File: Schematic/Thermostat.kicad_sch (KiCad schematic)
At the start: 36 parts, among them J1 Relay conn., J2 Thermocouple, J4 USB_B_Micro, J5 Firmware, K1 SONGLE_SRD_05VDC_SL_C, Q1 BSS138, SW1 Reset, SW2 Temp+, SW3 Preset1, SW4 Temp-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

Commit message: Added status LEDs, changed button functions
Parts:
- added D2: Green, LED_SMD:LED_0603_1608Metric_Pad1.05x0.95mm_HandSolder, symbol Device:LED_Small
- added D3: Red, LED_SMD:LED_0603_1608Metric_Pad1.05x0.95mm_HandSolder, symbol Device:LED_Small
- added H1, H2: MountingHole, MountingHole:MountingHole_3.2mm_M3, symbol Mechanical:MountingHole
- added R23 (x2): 1kΩ, Resistor_SMD:R_0603_1608Metric_Pad0.98x0.95mm_HandSolder, symbol Device:R_Small
- D4: renamed from D3; value "+5V" -> Green
- J5: footprint myDevices:PinHeader_1x06_P2.54mm_Vertical_Minus2 -> Retronics_Connectors:PinHeader_1x06_P2.54mm_Vertical_Minus2
- SW6: value Function -> Enter
- SW7: value Hysteresis -> Setup
- renumbered SW4 to SW3, SW3 to SW4
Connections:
- net GND: now also D2.1 (K), D3.1 (K)
- net LED_TEMP: now reaches U2.25 (A2)
- net LED_TEMP: now also R23.1
- net LED_STATUS: now reaches U2.26 (A3)
- net LED_STATUS: now also R23.1
- net SW_Function renamed SW_Enter
- net SW_Hysteresis renamed SW_Setup
- new net: D3.2 (A), R23.2
- new net: D2.2 (A), R23.2
- no-connect marks 13 -> 11

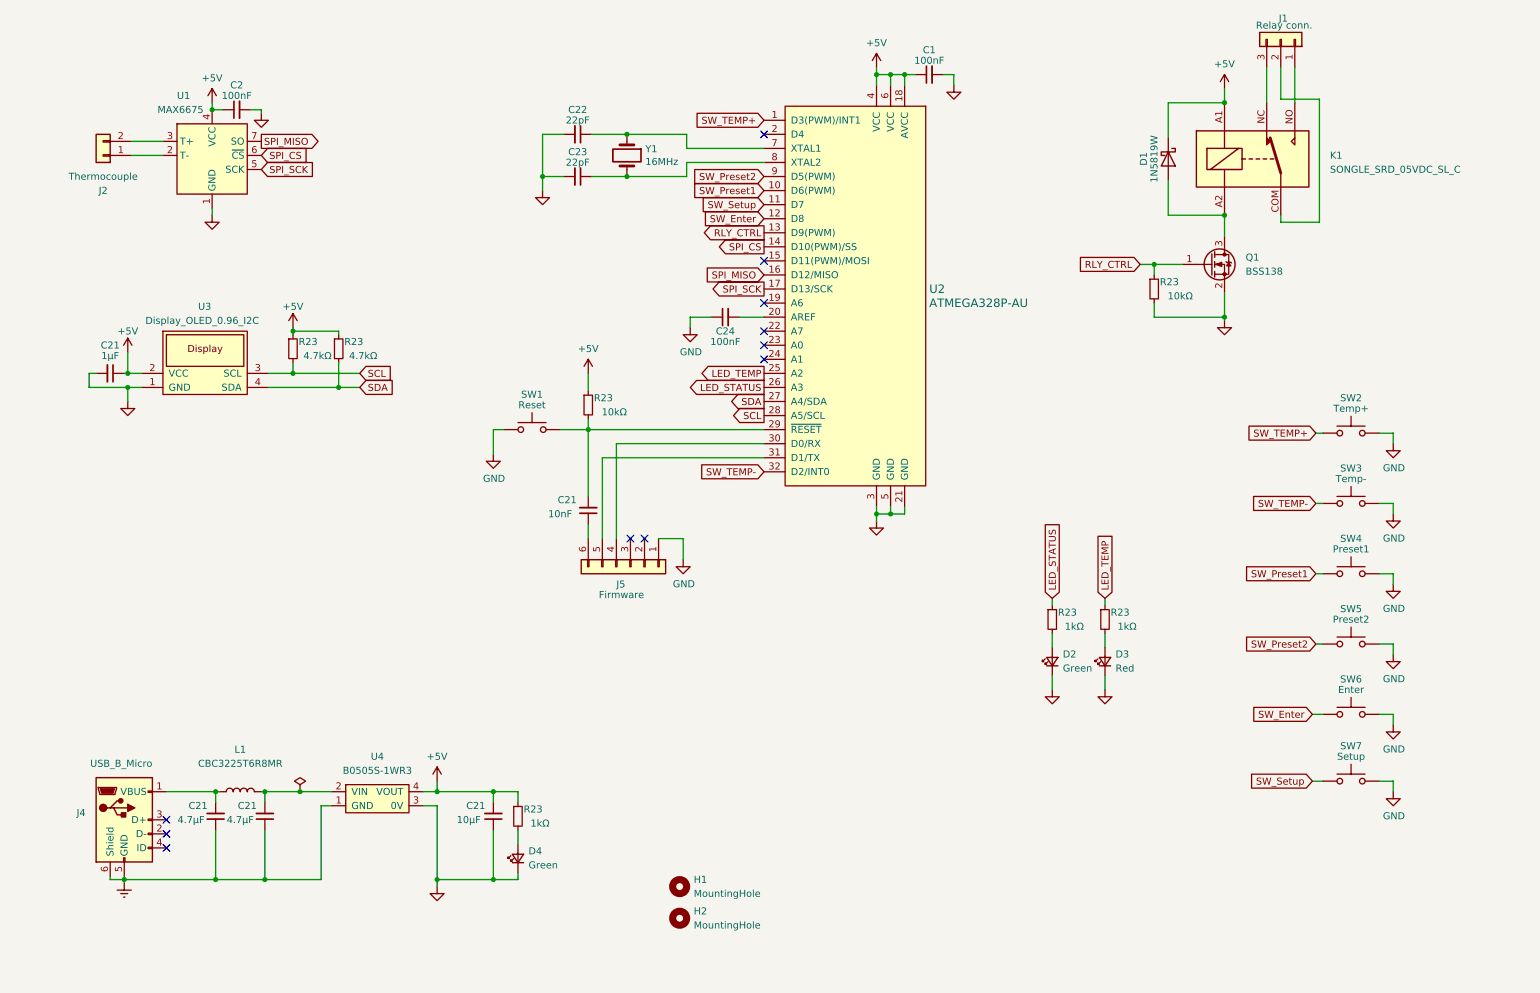
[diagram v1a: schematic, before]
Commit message: Added pull-up/pull-down resistors for sensor, removed redundant LEDs
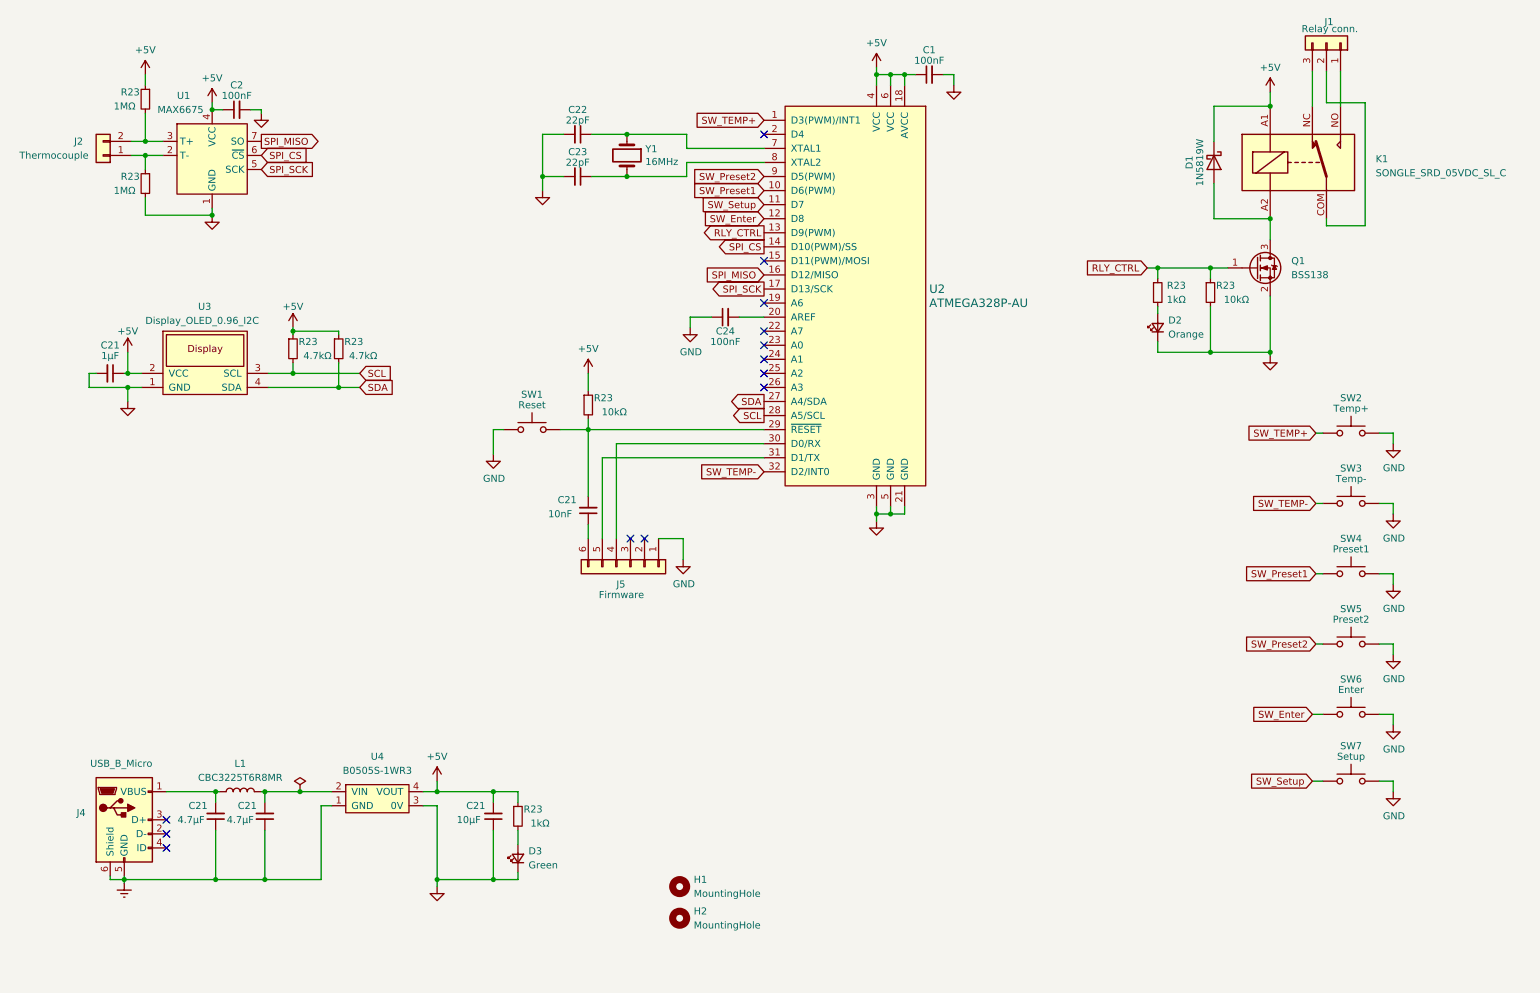
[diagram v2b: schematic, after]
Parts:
- removed D3: Red, LED_SMD:LED_0603_1608Metric_Pad1.05x0.95mm_HandSolder, symbol Device:LED_Small
- removed R23 (x2): 1kΩ, Resistor_SMD:R_0603_1608Metric_Pad0.98x0.95mm_HandSolder, symbol Device:R_Small
- added R23: 1kΩ, Resistor_SMD:R_0603_1608Metric_Pad0.98x0.95mm_HandSolder, symbol Device:R_Small
- added R23 (x2): 1MΩ, Resistor_SMD:R_0603_1608Metric_Pad0.98x0.95mm_HandSolder, symbol Device:R_Small
- D2: value Green -> Orange
- renumbered D4 to D3
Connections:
- net +5V: now also R23.1
- net GND: now also R23.2
- net RLY_CTRL: now also R23.1
- net at D2.2 (A): now also R23.2
- net at J2.1 (Pin_1), U1.2 (T-): now also R23.1
- net at J2.2 (Pin_2), U1.3 (T+): now also R23.2
- net LED_STATUS: no longer names the net of U2.26 (A3)
- net LED_TEMP: no longer names the net of U2.25 (A2)
- no-connect marks 11 -> 13
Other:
- moved on the sheet: D1, J1, K1, Q1, R23

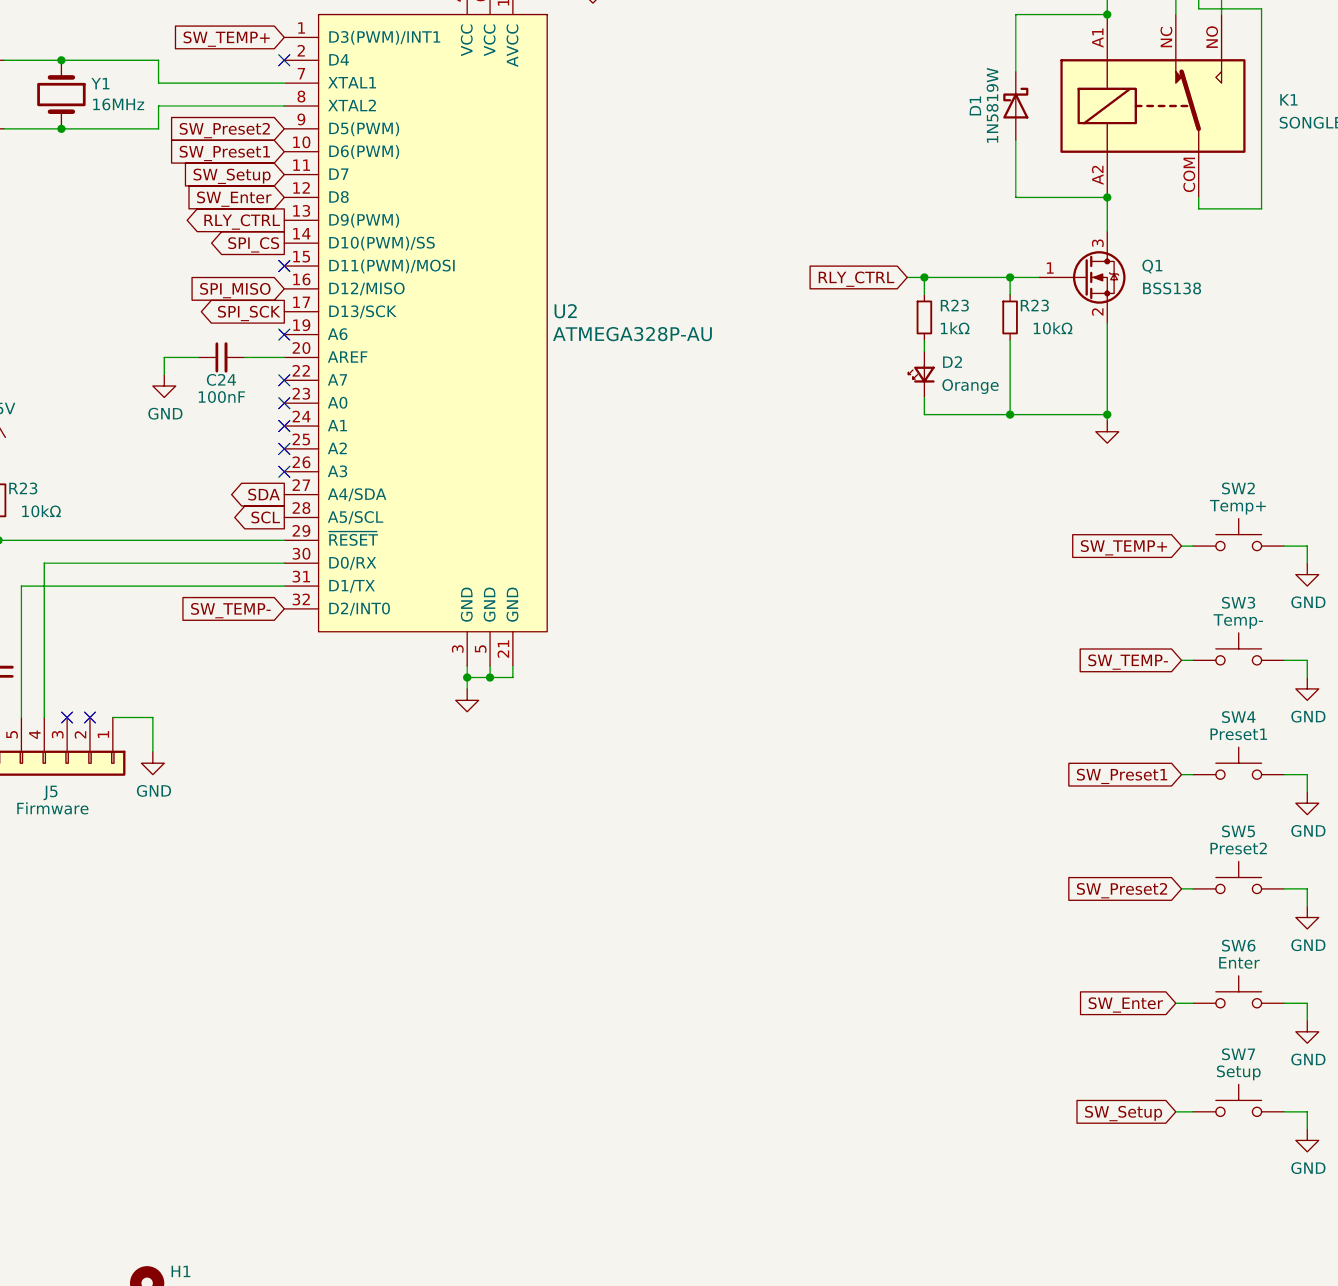
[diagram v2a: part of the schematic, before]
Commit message: Altered button configuration
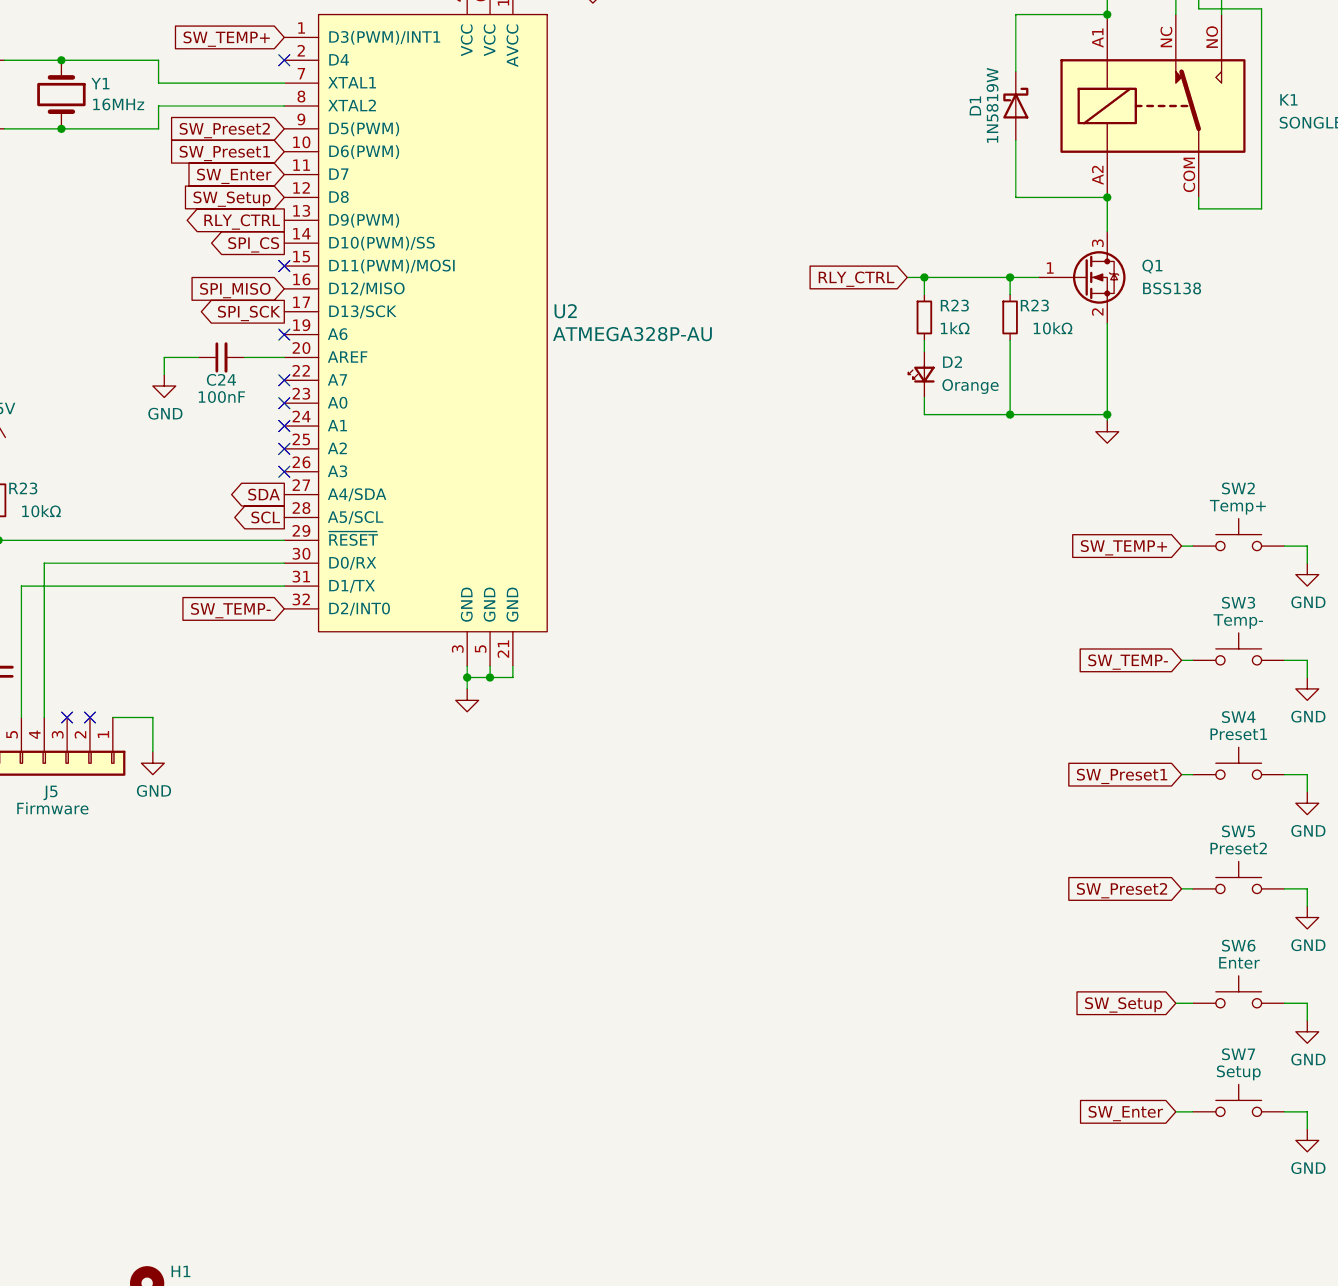
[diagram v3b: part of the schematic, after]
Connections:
- net SW_Enter: now also SW7.1, U2.11 (D7); no longer SW6.1, U2.12 (D8)
- net SW_Setup: now also SW6.1, U2.12 (D8); no longer SW7.1, U2.11 (D7)
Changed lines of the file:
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@@
     )
   )
-  (global_label "SW_Enter" (shape input) (at 149.86 52.07 180) (fields_autoplaced)
+  (global_label "SW_Enter" (shape input) (at 149.86 49.53 180) (fields_autoplaced)
     (effects (font (size 1.27 1.27)) (justify right))
-    (property "Intersheetrefs" "${INTERSHEET_REFS}" (at 138.3478 52.07 0)
+    (property "Intersheetrefs" "${INTERSHEET_REFS}" (at 138.3478 49.53 0)
       (effects (font (size 1.27 1.27)) (justify right) hide)
     )
@@
     )
   )
-  (global_label "SW_Enter" (shape input) (at 248.92 141.605 180) (fields_autoplaced)
+  (global_label "SW_Enter" (shape input) (at 248.92 153.67 180) (fields_autoplaced)
     (effects (font (size 1.27 1.27)) (justify right))
-    (property "Intersheetrefs" "${INTERSHEET_REFS}" (at 237.4078 141.605 0)
+    (property "Intersheetrefs" "${INTERSHEET_REFS}" (at 237.4078 153.67 0)
       (effects (font (size 1.27 1.27)) (justify right) hide)
     )
@@
     )
   )
-  (global_label "SW_Setup" (shape input) (at 248.92 153.67 180) (fields_autoplaced)
+  (global_label "SW_Setup" (shape input) (at 248.92 141.605 180) (fields_autoplaced)
     (effects (font (size 1.27 1.27)) (justify right))
-    (property "Intersheetrefs" "${INTERSHEET_REFS}" (at 236.9845 153.67 0)
+    (property "Intersheetrefs" "${INTERSHEET_REFS}" (at 236.9845 141.605 0)
       (effects (font (size 1.27 1.27)) (justify right) hide)
     )
@@
     )
   )
-  (global_label "SW_Setup" (shape input) (at 149.86 49.53 180) (fields_autoplaced)
+  (global_label "SW_Setup" (shape input) (at 149.86 52.07 180) (fields_autoplaced)
     (effects (font (size 1.27 1.27)) (justify right))
-    (property "Intersheetrefs" "${INTERSHEET_REFS}" (at 137.9245 49.53 0)
+    (property "Intersheetrefs" "${INTERSHEET_REFS}" (at 137.9245 52.07 0)
       (effects (font (size 1.27 1.27)) (justify right) hide)
     )
